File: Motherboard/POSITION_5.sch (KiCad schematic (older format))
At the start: 31 parts, among them Q20 MOSFET_N_(2N7002P,215), Q21 MOSFET_N_(2N7002P,215), Q22 MOSFET_N_(FDMA430NZ), Q23 MOSFET_P_(BS250FTA)

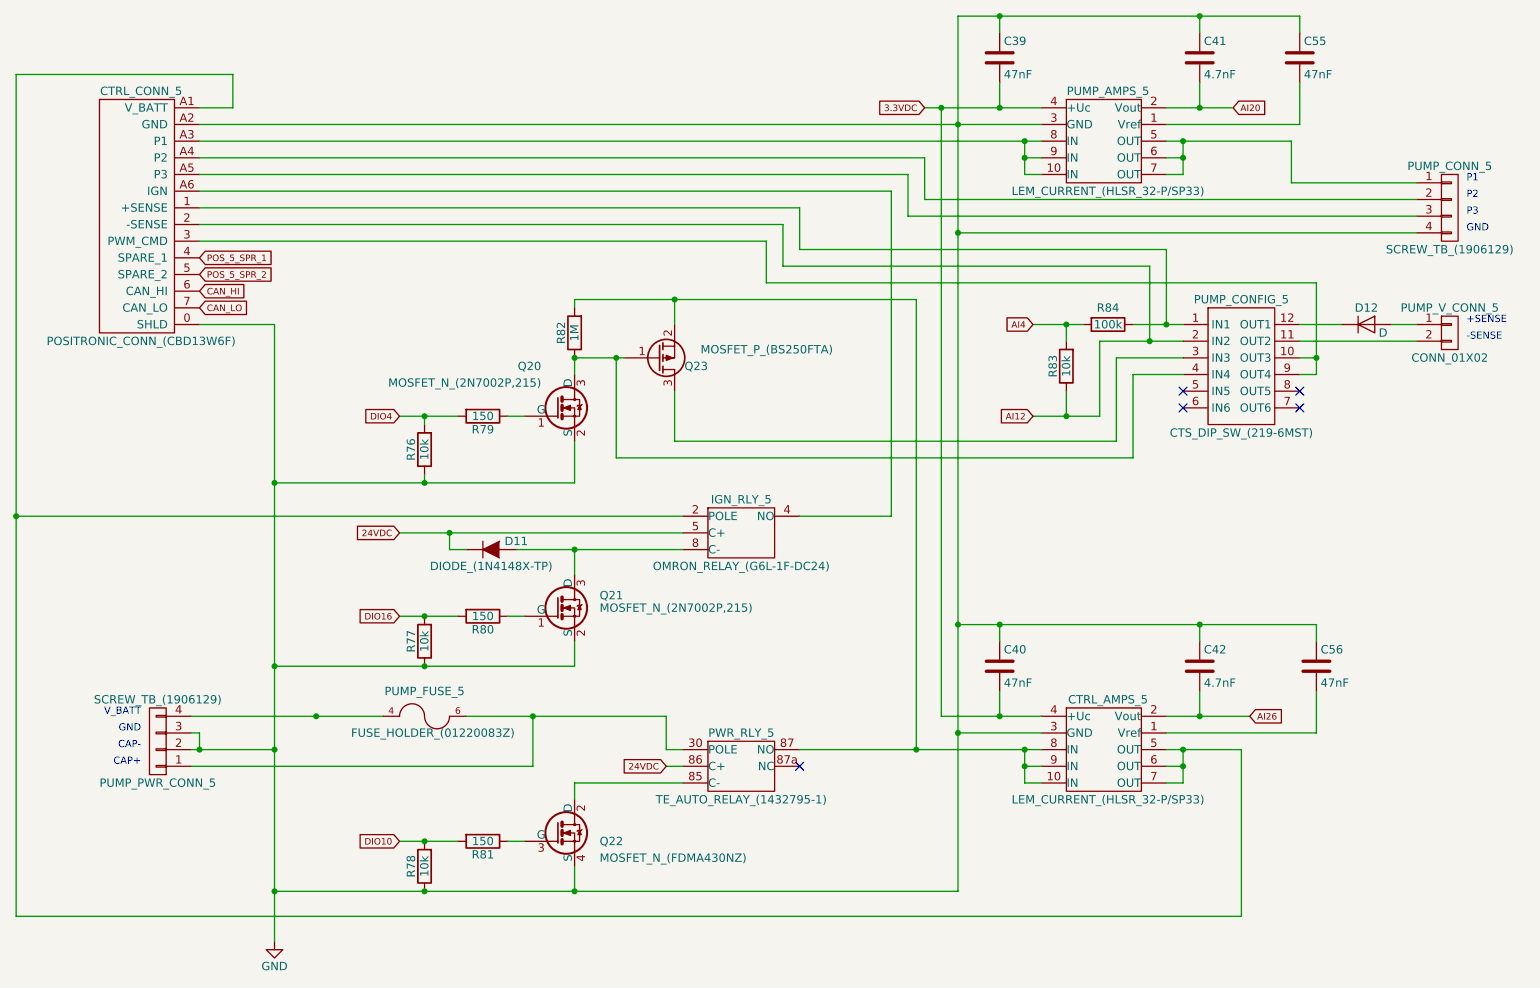
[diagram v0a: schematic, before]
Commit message: - Refer to Google Drive BOM for list of changes for v1.1 - Create drawing for Hella BLDC controller plate.
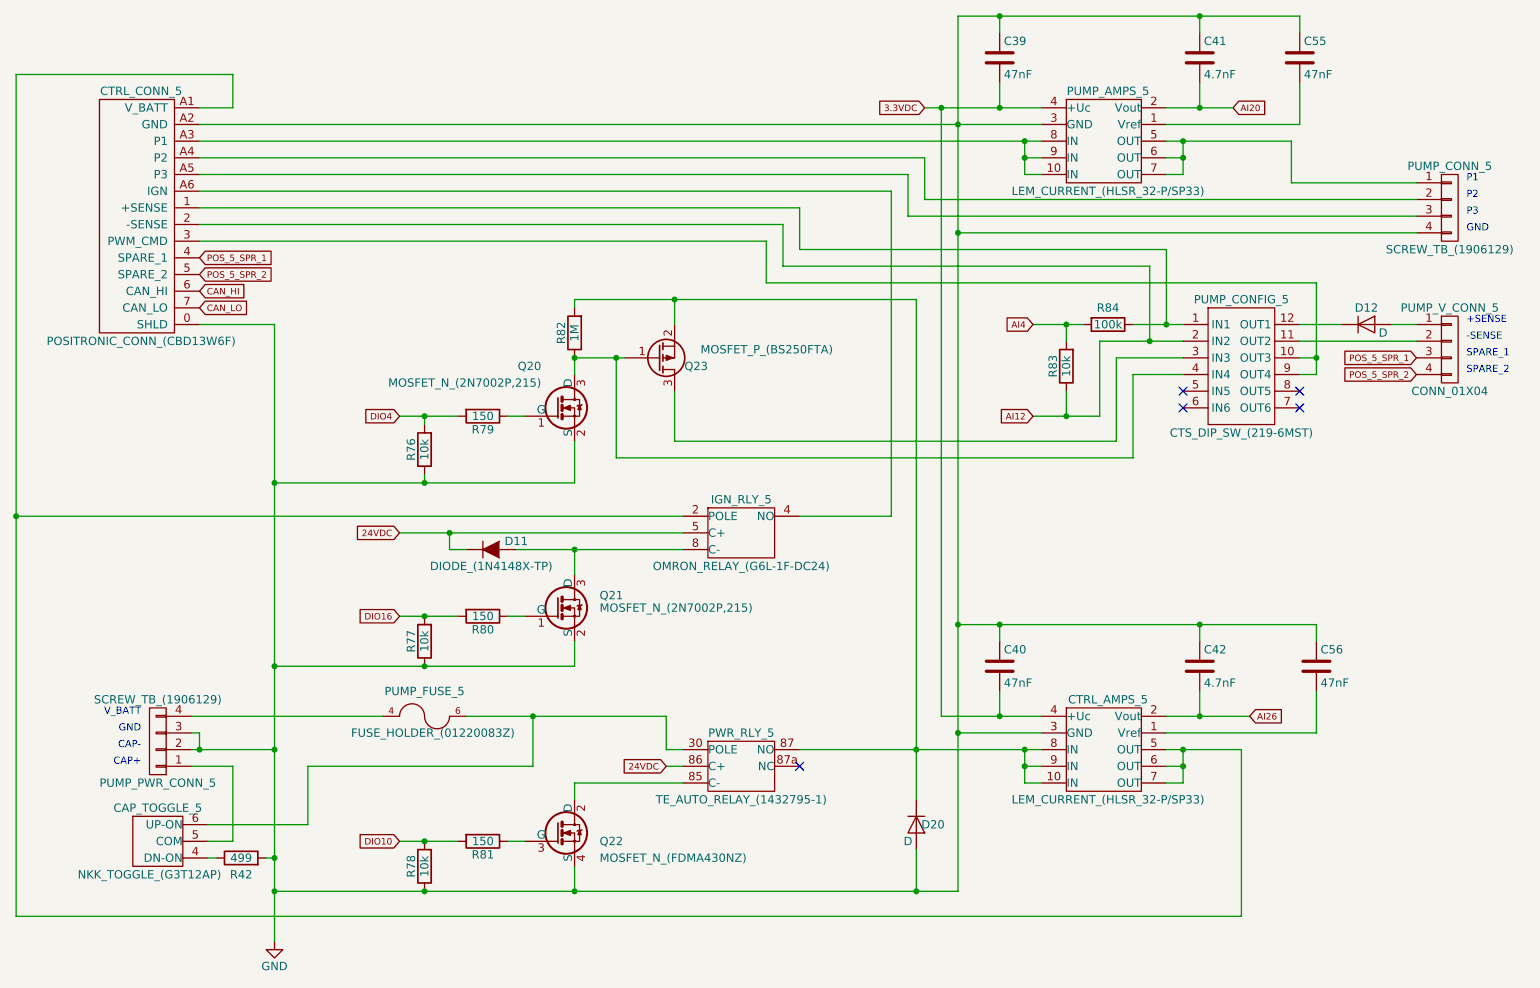
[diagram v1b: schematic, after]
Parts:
- removed PUMP_V_CONN_5: CONN_01X02, Smart_Tank:PHNX_TB_SCREW_2_POS_(1729128), symbol CONN_01X02
- added CAP_TOGGLE_5: NKK_TOGGLE_(G3T12AP), Smart_Tank:NKK_TOGGLE_(G3T12AP), symbol NKK_TOGGLE_(G3T12AP)
- added D20: D, Diodes_SMD:D_SOD-123, symbol D
- added PUMP_V_CONN_5: CONN_01X04, Smart_Tank:PHNX_TB_SCREW_4_POS_(1729144), symbol CONN_01X04
- added R42: 499, Resistors_SMD:R_1206, symbol R
- D12: footprint Diodes_SMD:SOD-523 -> Diodes_SMD:SOD-123
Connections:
- net GND: now also D20.2 (A), R42.2
- net POS_5_SPR_1: now also PUMP_V_CONN_5.3 (P3)
- net POS_5_SPR_2: now also PUMP_V_CONN_5.4 (P4)
- net at PUMP_FUSE_5.6, PUMP_FUSE_5.7, PWR_RLY_5.30 (POLE): now also CAP_TOGGLE_5.6 (UP-ON); no longer PUMP_PWR_CONN_5.1 (P1)
- net at CTRL_AMPS_5.10 (IN), CTRL_AMPS_5.8 (IN), CTRL_AMPS_5.9 (IN)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: now also D20.1 (K)
- net at PUMP_CONFIG_5.11 (OUT2): now also PUMP_V_CONN_5.2 (P2)
- net at D12.2 (A): now also PUMP_V_CONN_5.1 (P1)
- new net: CAP_TOGGLE_5.5 (COM), PUMP_PWR_CONN_5.1 (P1)
- new net: CAP_TOGGLE_5.4 (DN-ON), R42.1
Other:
- note added: "SPARE_1"
- note added: "SPARE_2"
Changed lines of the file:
@@
 CAP+
 $Comp
-L GND #PWR025
+L GND #PWR026
 U 1 1 57A93EB7
 P 2950 6350
-F 0 "#PWR025" H 2950 6100 50  0001 C CNN
+F 0 "#PWR026" H 2950 6100 50  0001 C CNN
 F 1 "GND" H 2950 6200 50  0000 C CNN
 F 2 "" H 2950 6350 50  0000 C CNN
@@
 	1    0    0    -1
 $EndComp
-$Comp
-L CONN_01X02 PUMP_V_CONN_5
-U 1 1 57A93F73
-P 10000 2700
-F 0 "PUMP_V_CONN_5" H 10000 2850 50  0000 C CNN
-F 1 "CONN_01X02" H 10000 2550 50  0000 C CNN
-F 2 "Smart_Tank:PHNX_TB_SCREW_2_POS_(1729128)" H 10000 2700 50  0001 C CNN
-F 3 "" H 10000 2700 50  0000 C CNN
-	1    10000 2700
-	1    0    0    -1
-$EndComp
 Text Notes 10100 2650 0    43   ~ 0
 +SENSE
@@
 	2500 5100 2500 5200
 Connection ~ 2500 5200
-Wire Wire Line
-	4500 5300 2450 5300
 Connection ~ 4500 5000
 Wire Wire Line
@@
 	4750 2500 6800 2500
 Wire Wire Line
-	6800 2500 6800 5200
+	6800 2500 6800 5500
 Connection ~ 6800 5200
 Wire Wire Line
@@
 	2950 4700 4750 4700
 Connection ~ 3850 4700
-Connection ~ 3200 5000
 Connection ~ 2950 6050
 Wire Wire Line
@@
 F 0 "D12" H 9500 2750 50  0000 C CNN
 F 1 "D" H 9600 2600 50  0000 C CNN
-F 2 "Diodes_SMD:SOD-523" H 9500 2650 50  0001 C CNN
+F 2 "Diodes_SMD:SOD-123" H 9500 2650 50  0001 C CNN
 F 3 "" H 9500 2650 50  0000 C CNN
 	1    9500 2650
@@
 	9200 4450 9200 4550
 Connection ~ 8500 4450
+$Comp
+L NKK_TOGGLE_(G3T12AP) CAP_TOGGLE_5
+U 1 1 5976CD51
+P 2250 5750
+F 0 "CAP_TOGGLE_5" H 2250 5950 50  0000 C CNN
+F 1 "NKK_TOGGLE_(G3T12AP)" H 2200 5550 50  0000 C CNN
+F 2 "Smart_Tank:NKK_TOGGLE_(G3T12AP)" H 2250 4550 50  0001 C CNN
+F 3 "" H 2250 4550 50  0000 C CNN
+	1    2250 5750
+	1    0    0    -1
+$EndComp
+Wire Wire Line
+	2450 5300 2700 5300
+Wire Wire Line
+	3150 5300 4500 5300
+$Comp
+L D D20
+U 1 1 5976DA03
+P 6800 5650
+F 0 "D20" V 6800 5750 50  0000 C CNN
+F 1 "D" V 6900 5600 50  0000 C CNN
+F 2 "Diodes_SMD:D_SOD-123" H 6800 5650 50  0001 C CNN
+F 3 "" H 6800 5650 50  0000 C CNN
+	1    6800 5650
+	0    1    1    0
+$EndComp
+Wire Wire Line
+	6800 5800 6800 6050
+Connection ~ 6800 6050
+$Comp
+L R R42
+U 1 1 5978D775
+P 2750 5850
+F 0 "R42" V 2650 5850 50  0000 C CNN
+F 1 "499" V 2750 5850 50  0000 C CNN
+F 2 "Resistors_SMD:R_1206" V 2680 5850 50  0001 C CNN
+F 3 "" H 2750 5850 50  0000 C CNN
+	1    2750 5850
+	0    -1   -1   0
+$EndComp
+Wire Wire Line
+	2550 5750 2700 5750
+Wire Wire Line
+	2700 5750 2700 5300
+Wire Wire Line
+	2550 5650 3150 5650
+Wire Wire Line
+	3150 5650 3150 5300
+Wire Wire Line
+	2550 5850 2600 5850
+Wire Wire Line
+	2900 5850 2950 5850
+Connection ~ 2950 5850
+$Comp
+L CONN_01X04 PUMP_V_CONN_5
+U 1 1 5979B1F5
+P 10000 2800
+F 0 "PUMP_V_CONN_5" H 10000 3050 50  0000 C CNN
+F 1 "CONN_01X04" H 10000 2550 50  0000 C CNN
+F 2 "Smart_Tank:PHNX_TB_SCREW_4_POS_(1729144)" H 10000 2800 50  0001 C CNN
+F 3 "" H 10000 2800 50  0001 C CNN
+	1    10000 2800
+	1    0    0    -1
+$EndComp
+Text GLabel 9800 2850 0    39   Input ~ 0
+POS_5_SPR_1
+Text GLabel 9800 2950 0    39   Input ~ 0
+POS_5_SPR_2
+Text Notes 10100 2850 0    43   ~ 0
+SPARE_1
+Text Notes 10100 2950 0    43   ~ 0
+SPARE_2
 $EndSCHEMATC

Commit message: - Created Modbus Adapter.
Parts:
- C39, C40, C41, C42, C55, C56: symbol C -> Smart-Tank-Motherboard-rescue:C
- CAP_TOGGLE_5: symbol NKK_TOGGLE_(G3T12AP) -> Smart-Tank-Motherboard-rescue:NKK_TOGGLE_(G3T12AP)
- CTRL_AMPS_5, PUMP_AMPS_5: symbol LEM_CURRENT_(HLSR_32-P/SP33) -> Smart-Tank-Motherboard-rescue:LEM_CURRENT_(HLSR_32-P_SP33)
- CTRL_CONN_5: symbol POSITRONIC_CONN_(CBD13W6F) -> Smart-Tank-Motherboard-rescue:POSITRONIC_CONN_(CBD13W6F)
- D11: symbol DIODE_(1N4148X-TP) -> Smart-Tank-Motherboard-rescue:DIODE_(1N4148X-TP)
- D12, D20: symbol D -> Smart-Tank-Motherboard-rescue:D
- IGN_RLY_5: symbol OMRON_RELAY_(G6L-1F-DC24) -> Smart-Tank-Motherboard-rescue:OMRON_RELAY_(G6L-1F-DC24)
- PUMP_CONFIG_5: symbol CTS_DIP_SW_(219-6MST) -> Smart-Tank-Motherboard-rescue:CTS_DIP_SW_(219-6MST)
- PUMP_CONN_5, PUMP_PWR_CONN_5: symbol SCREW_TB_(1906129) -> Smart-Tank-Motherboard-rescue:SCREW_TB_(1906129)
- PUMP_FUSE_5: symbol FUSE_HOLDER_(01220083Z) -> Smart-Tank-Motherboard-rescue:FUSE_HOLDER_(01220083Z)
- PUMP_V_CONN_5: symbol CONN_01X04 -> Smart-Tank-Motherboard-rescue:CONN_01X04
- PWR_RLY_5: symbol TE_AUTO_RELAY_(1432795-1) -> Smart-Tank-Motherboard-rescue:TE_AUTO_RELAY_(1432795-1)
- Q20, Q21: symbol MOSFET_N_(2N7002P,215) -> Smart-Tank-Motherboard-rescue:MOSFET_N_(2N7002P,215)
- Q22: symbol MOSFET_N_(FDMA430NZ) -> Smart-Tank-Motherboard-rescue:MOSFET_N_(FDMA430NZ)
- Q23: symbol MOSFET_P_(BS250FTA) -> Smart-Tank-Motherboard-rescue:MOSFET_P_(BS250FTA)
- R42, R76, R77, R78, R79, R80, R81, R82, R83, R84: symbol R -> Smart-Tank-Motherboard-rescue:R
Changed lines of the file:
@@
-EESchema Schematic File Version 2
-LIBS:Smart Tank Motherboard-rescue
-LIBS:power
-LIBS:device
-LIBS:transistors
-LIBS:conn
-LIBS:linear
-LIBS:regul
-LIBS:74xx
-LIBS:cmos4000
-LIBS:adc-dac
-LIBS:memory
-LIBS:xilinx
-LIBS:microcontrollers
-LIBS:dsp
-LIBS:microchip
-LIBS:analog_switches
-LIBS:motorola
-LIBS:texas
-LIBS:intel
-LIBS:audio
-LIBS:interface
-LIBS:digital-audio
-LIBS:philips
-LIBS:display
-LIBS:cypress
-LIBS:siliconi
-LIBS:opto
-LIBS:atmel
-LIBS:contrib
-LIBS:valves
+EESchema Schematic File Version 4
 LIBS:Smart Tank Motherboard-cache
-EELAYER 25 0
+EELAYER 29 0
 EELAYER END
 $Descr A4 11693 8268
@@
 $EndDescr
 $Comp
-L R R81
+L Smart-Tank-Motherboard-rescue:R R81
 U 1 1 57A93E9D
 P 4200 5750
@@
 $EndComp
 $Comp
-L R R78
+L Smart-Tank-Motherboard-rescue:R R78
 U 1 1 57A93EA4
 P 3850 5900
@@
 $EndComp
 $Comp
-L SCREW_TB_(1906129) PUMP_PWR_CONN_5
+L Smart-Tank-Motherboard-rescue:SCREW_TB_(1906129) PUMP_PWR_CONN_5
 U 1 1 57A93EAC
 P 2250 5150
@@
 CAP+
 $Comp
-L GND #PWR026
+L Smart-Tank-Motherboard-rescue:GND #PWR026
 U 1 1 57A93EB7
 P 2950 6350
@@
 $EndComp
 $Comp
-L SCREW_TB_(1906129) PUMP_CONN_5
+L Smart-Tank-Motherboard-rescue:SCREW_TB_(1906129) PUMP_CONN_5
 U 1 1 57A93ECC
 P 10000 1950
@@
 GND
 $Comp
-L POSITRONIC_CONN_(CBD13W6F) CTRL_CONN_5
+L Smart-Tank-Motherboard-rescue:POSITRONIC_CONN_(CBD13W6F) CTRL_CONN_5
 U 1 1 57A93ED7
 P 2150 1900
@@
 $EndComp
 $Comp
-L FUSE_HOLDER_(01220083Z) PUMP_FUSE_5
+L Smart-Tank-Motherboard-rescue:FUSE_HOLDER_(01220083Z) PUMP_FUSE_5
 U 1 1 57A93EDE
 P 3850 5000
@@
 $EndComp
 $Comp
-L MOSFET_N_(FDMA430NZ) Q22
+L Smart-Tank-Motherboard-rescue:MOSFET_N_(FDMA430NZ) Q22
 U 1 1 57A93EE5
 P 4650 5700
@@
 $EndComp
 $Comp
-L TE_AUTO_RELAY_(1432795-1) PWR_RLY_5
+L Smart-Tank-Motherboard-rescue:TE_AUTO_RELAY_(1432795-1) PWR_RLY_5
 U 1 1 57A93EEC
 P 5650 5400
@@
 AI26
 $Comp
-L OMRON_RELAY_(G6L-1F-DC24) IGN_RLY_5
+L Smart-Tank-Motherboard-rescue:OMRON_RELAY_(G6L-1F-DC24) IGN_RLY_5
 U 1 1 57A93EF8
 P 5650 4000
@@
 $EndComp
 $Comp
-L MOSFET_N_(2N7002P,215) Q21
+L Smart-Tank-Motherboard-rescue:MOSFET_N_(2N7002P,215) Q21
 U 1 1 57A93EFF
 P 4650 4350
@@
 $EndComp
 $Comp
-L R R80
+L Smart-Tank-Motherboard-rescue:R R80
 U 1 1 57A93F06
 P 4200 4400
@@
 $EndComp
 $Comp
-L R R77
+L Smart-Tank-Motherboard-rescue:R R77
 U 1 1 57A93F0D
 P 3850 4550
@@
 CAN_LO
 $Comp
-L DIODE_(1N4148X-TP) D11
+L Smart-Tank-Motherboard-rescue:DIODE_(1N4148X-TP) D11
 U 1 1 57A93F18
 P 4250 4000
@@
 POS_5_SPR_2
 $Comp
-L MOSFET_N_(2N7002P,215) Q20
+L Smart-Tank-Motherboard-rescue:MOSFET_N_(2N7002P,215) Q20
 U 1 1 57A93F21
 P 4650 3150
@@
 $EndComp
 $Comp
-L MOSFET_P_(BS250FTA) Q23
+L Smart-Tank-Motherboard-rescue:MOSFET_P_(BS250FTA) Q23
 U 1 1 57A93F28
 P 5250 2850
@@
 $EndComp
 $Comp
-L R R79
+L Smart-Tank-Motherboard-rescue:R R79
 U 1 1 57A93F2F
 P 4200 3200
@@
 $EndComp
 $Comp
-L R R82
+L Smart-Tank-Motherboard-rescue:R R82
 U 1 1 57A93F36
 P 4750 2700
@@
 DIO4
 $Comp
-L R R76
+L Smart-Tank-Motherboard-rescue:R R76
 U 1 1 57A93F3E
 P 3850 3400
@@
 NoConn ~ 6100 5300
 $Comp
-L C C41
+L Smart-Tank-Motherboard-rescue:C C41
 U 1 1 57A93F50
 P 8500 1050
@@
 $EndComp
 $Comp
-L C C39
+L Smart-Tank-Motherboard-rescue:C C39
 U 1 1 57A93F57
 P 7300 1050
@@
 $EndComp
 $Comp
-L C C42
+L Smart-Tank-Motherboard-rescue:C C42
 U 1 1 57A93F5E
 P 8500 4700
@@
 $EndComp
 $Comp
-L C C40
+L Smart-Tank-Motherboard-rescue:C C40
 U 1 1 57A93F65
 P 7300 4700
@@
 $EndComp
 $Comp
-L CTS_DIP_SW_(219-6MST) PUMP_CONFIG_5
+L Smart-Tank-Motherboard-rescue:CTS_DIP_SW_(219-6MST) PUMP_CONFIG_5
 U 1 1 57A93F6C
 P 8750 2900
@@
 NoConn ~ 8400 3150
 $Comp
-L R R83
+L Smart-Tank-Motherboard-rescue:R R83
 U 1 1 57A93F80
 P 7700 2900
@@
 $EndComp
 $Comp
-L R R84
+L Smart-Tank-Motherboard-rescue:R R84
 U 1 1 57A93F87
 P 7950 2650
@@
 	4750 2550 4750 2500
 $Comp
-L D D12
+L Smart-Tank-Motherboard-rescue:D D12
 U 1 1 57A94045
 P 9500 2650
@@
 	9650 2650 9800 2650
 $Comp
-L LEM_CURRENT_(HLSR_32-P/SP33) PUMP_AMPS_5
+L Smart-Tank-Motherboard-rescue:LEM_CURRENT_(HLSR_32-P_SP33) PUMP_AMPS_5
 U 1 1 57B748D2
 P 7800 1550
@@
 $EndComp
 $Comp
-L LEM_CURRENT_(HLSR_32-P/SP33) CTRL_AMPS_5
+L Smart-Tank-Motherboard-rescue:LEM_CURRENT_(HLSR_32-P_SP33) CTRL_AMPS_5
 U 1 1 57B76EC9
 P 7800 5200
@@
 Connection ~ 2950 3600
 $Comp
-L C C55
+L Smart-Tank-Motherboard-rescue:C C55
 U 1 1 57D20040
 P 9100 1050
@@
 Connection ~ 8500 800
 $Comp
-L C C56
+L Smart-Tank-Motherboard-rescue:C C56
 U 1 1 57D2057D
 P 9200 4700
@@
 Connection ~ 8500 4450
 $Comp
-L NKK_TOGGLE_(G3T12AP) CAP_TOGGLE_5
+L Smart-Tank-Motherboard-rescue:NKK_TOGGLE_(G3T12AP) CAP_TOGGLE_5
 U 1 1 5976CD51
 P 2250 5750
@@
 	3150 5300 4500 5300
 $Comp
-L D D20
+L Smart-Tank-Motherboard-rescue:D D20
 U 1 1 5976DA03
 P 6800 5650
@@
 Connection ~ 6800 6050
 $Comp
-L R R42
+L Smart-Tank-Motherboard-rescue:R R42
 U 1 1 5978D775
 P 2750 5850
@@
 Connection ~ 2950 5850
 $Comp
-L CONN_01X04 PUMP_V_CONN_5
+L Smart-Tank-Motherboard-rescue:CONN_01X04 PUMP_V_CONN_5
 U 1 1 5979B1F5
 P 10000 2800
